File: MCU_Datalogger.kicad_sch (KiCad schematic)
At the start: 0 parts

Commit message: third
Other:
- title: (none) -> ${project_name}
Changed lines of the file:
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@@
 	(generator_version "10.0")
 	(paper "A4")
+	(title_block
+		(title "${project_name}")
+		(date "2026-07-26")
+		(rev "1")
+	)
 	(sheet_instances
 		(path "/"

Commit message: schematic 1
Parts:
- added BT1: Battery, symbol Device:Battery
- added C1, C2, C3, C4: C, symbol Device:C
- added C5: C_Polarized, symbol Device:C_Polarized
- added D1, D2: LED, symbol Device:LED
- added H1, H2, H3, H4: MountingHole, symbol Mechanical:MountingHole
- added R1, R2, R3, R4, R5, R6, R7: R, symbol Device:R
- added U1, U2: 24LC1025, symbol Memory_EEPROM:24LC1025
- added U3: DS1337S_, DS1337S_:SOIC127P600X175-8N, symbol DS1337S_:DS1337S_
- added U4: ATMEGA328P-AU, ATMEGA328P-AU:QFP80P900X900X120-32N, symbol ATMEGA328P-AU:ATMEGA328P-AU
- added Y1, Y2: Crystal, symbol Device:Crystal
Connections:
- new net GND: U4.21 (GND), U4.3 (GND), U4.5 (GND)
- new net VCC: U4.4 (VCC), U4.6 (VCC)

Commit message: aa
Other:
- added sheet Connectors (Connectors.kicad_sch)
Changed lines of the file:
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@@
+		)
+	)
+	(sheet
+		(at 110.744 142.24)
+		(size 39.624 37.084)
+		(exclude_from_sim no)
+		(in_bom yes)
+		(on_board yes)
+		(dnp no)
+		(fields_autoplaced yes)
+		(stroke
+			(width 0.1524)
+			(type solid)
+		)
+		(fill
+			(color 0 0 0 0)
+		)
+		(property "Sheetname" "Connectors"
+			(at 110.744 141.5284 0)
+			(show_name no)
+			(do_not_autoplace no)
+			(effects
+				(font
+					(size 1.27 1.27)
+				)
+				(justify left bottom)
+			)
+		)
+		(property "Sheetfile" "Connectors.kicad_sch"
+			(at 110.744 179.9086 0)
+			(show_name no)
+			(do_not_autoplace no)
+			(effects
+				(font
+					(size 1.27 1.27)
+				)
+				(justify left top)
+			)
+		)
+		(instances
+			(project "MCU_Datalogger"
+				(path "/14fc4073-58ef-4a71-a843-5cc47094620d"
+					(page "2")
+				)
+			)
 		)
 	)

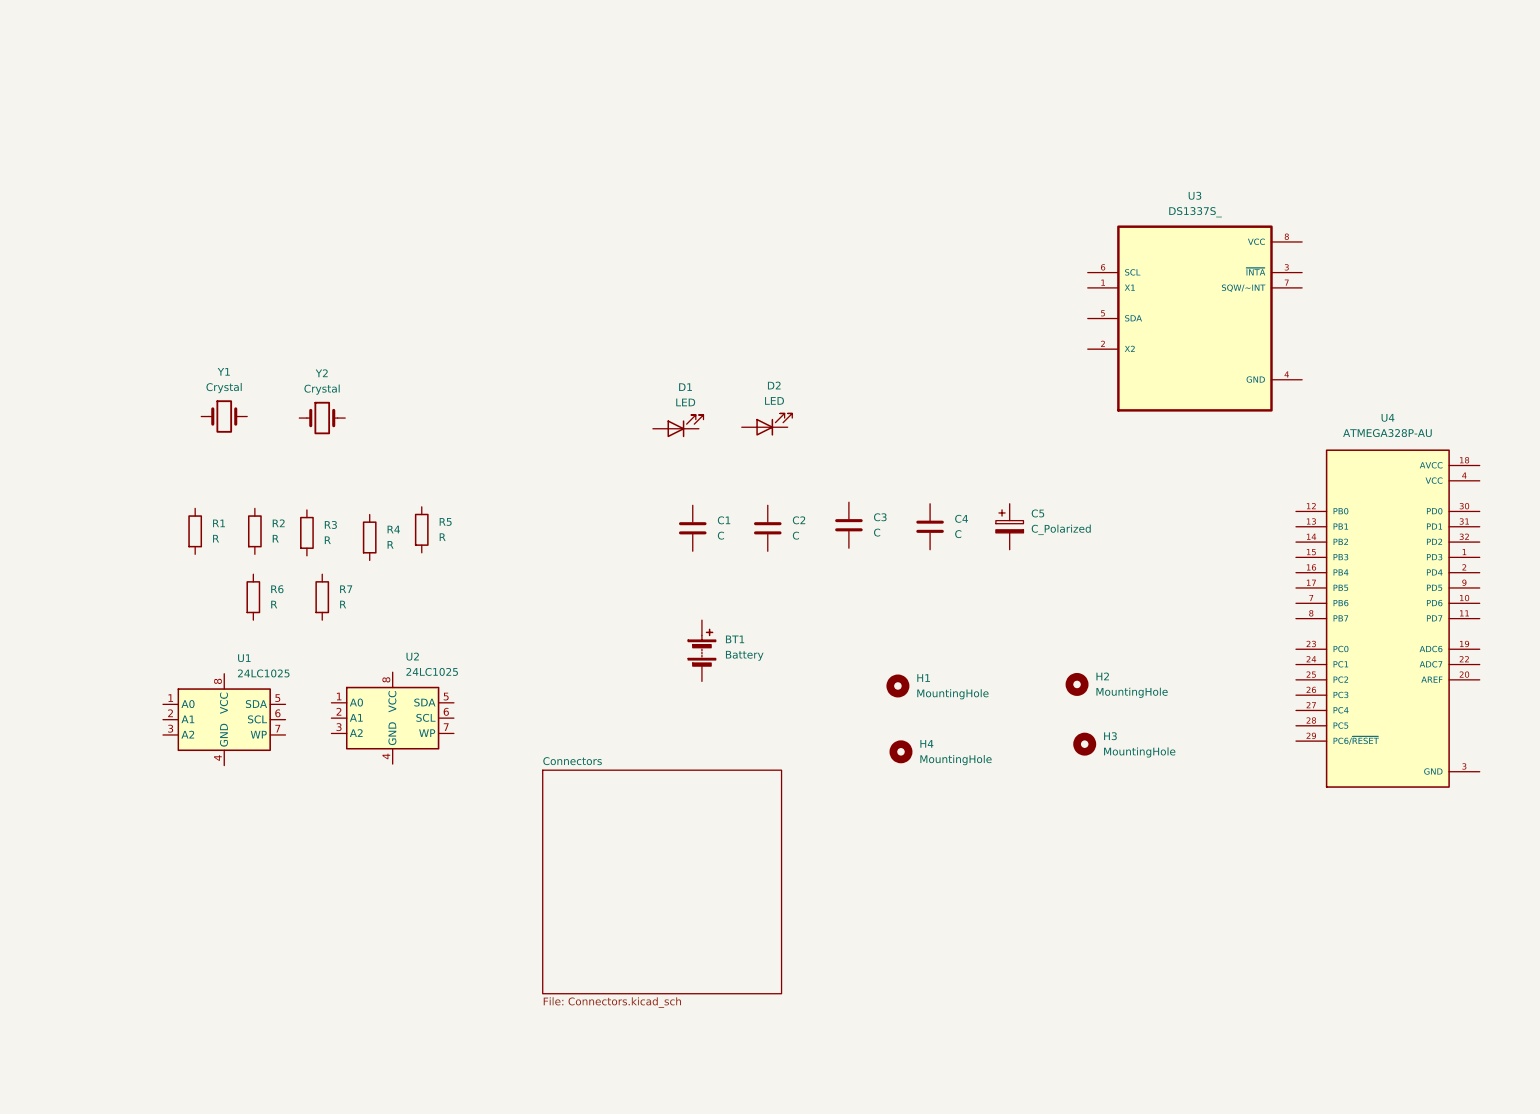
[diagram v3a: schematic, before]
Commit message: main schematic is wired
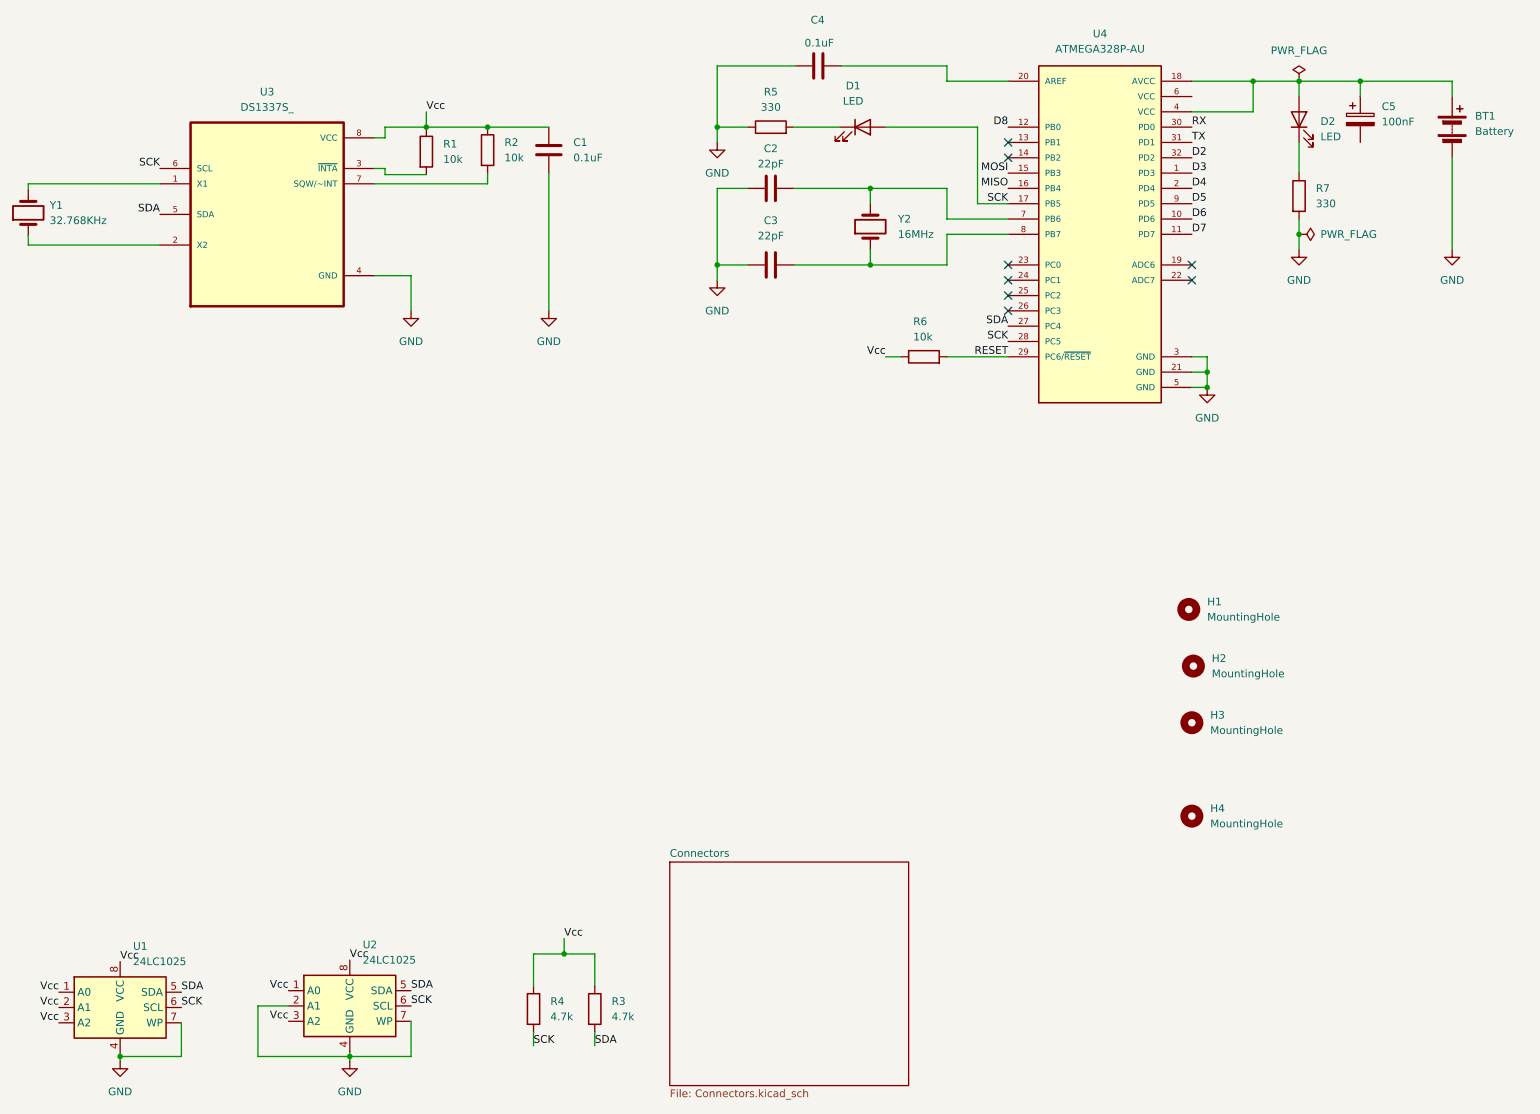
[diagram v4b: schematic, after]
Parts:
- BT1: footprint (none) -> Connector_PinHeader_2.54mm:PinHeader_1x02_P2.54mm_Vertical
- C1, C4: value C -> 0.1uF; footprint (none) -> Capacitor_SMD:C_0805_2012Metric
- C2, C3: value C -> 22pF; footprint (none) -> Capacitor_SMD:C_0805_2012Metric
- C5: value C_Polarized -> 100nF; footprint (none) -> Capacitor_SMD:C_0805_2012Metric
- D1, D2: footprint (none) -> Diode_SMD:D_0805_2012Metric
- H1, H2, H3, H4: footprint (none) -> MountingHole:MountingHole_2.1mm
- R1, R2, R6: value R -> 10k; footprint (none) -> Fuse:Fuse_0805_2012Metric
- R3, R4: value R -> 4.7k; footprint (none) -> Fuse:Fuse_0805_2012Metric
- R5, R7: value R -> 330; footprint (none) -> Fuse:Fuse_0805_2012Metric
- U1, U2: footprint (none) -> Package_SO:SOIC-8_5.3x5.3mm_P1.27mm
- U3: footprint DS1337S_:SOIC127P600X175-8N -> d1337s:SOIC127P600X175-8N
- U4: footprint ATMEGA328P-AU:QFP80P900X900X120-32N -> atmega3288p-au:QFP80P900X900X120-32N
- Y1: value Crystal -> 32.768KHz; footprint (none) -> Crystal:Crystal_SMD_5032-2Pin_5.0x3.2mm_HandSoldering
- Y2: value Crystal -> 16MHz; footprint (none) -> Crystal:Crystal_SMD_5032-2Pin_5.0x3.2mm_HandSoldering
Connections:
- net GND: now also BT1.2 (-), C1.2, C2.1, C3.2, C4.1, R5.1, R7.2, U1.4 (GND), U1.7 (WP), U2.2 (A1), U2.4 (GND), U2.7 (WP), U3.4 (GND)
- net at C3.1: now also U4.8 (PB7), Y2.1
- net Vcc: now reaches U1.1 (A0)
- net Vcc: now also C1.1, R1.1, R2.1, R3.1, R4.1, R6.1, U1.2 (A1), U1.3 (A2), U1.8 (VCC), U2.1 (A0), U2.3 (A2), U2.8 (VCC), U3.8 (VCC)
- net SDA: now reaches U1.5 (SDA)
- net SDA: now also R3.2, U2.5 (SDA), U3.5 (SDA), U4.27 (PC4)
- net SCK: now reaches U1.6 (SCL)
- net SCK: now also D1.2 (A), R4.2, U2.6 (SCL), U3.6 (SCL), U4.17 (PB5), U4.28 (PC5)
- net RESET: now reaches R6.2
- net RESET: now also U4.29 (PC6/~{RESET})
- net at Y1.1: now also U3.2 (X2)
- net at Y1.2: now also U3.1 (X1)
- net at C5.1: now also BT1.1 (+), D2.2 (A), U4.18 (AVCC), U4.4 (VCC)
- net at D1.1 (K): now also R5.2
- net at U3.3 (~{INTA}): now also R1.2
- net at U3.7 (SQW/~INT): now also R2.2
- net D3: now reaches U4.1 (PD3)
- net D6: now reaches U4.10 (PD6)
- net D7: now reaches U4.11 (PD7)
- net D8: now reaches U4.12 (PB0)
- net MOSI: now reaches U4.15 (PB3)
- net MISO: now reaches U4.16 (PB4)
- net D4: now reaches U4.2 (PD4)
- net at U4.20 (AREF): now also C4.2
- net RX: now reaches U4.30 (PD0)
- net TX: now reaches U4.31 (PD1)
- net D2: now reaches U4.32 (PD2)
- net at U4.7 (PB6): now also C2.2, Y2.2
- net D5: now reaches U4.9 (PD5)
- net at D2.1 (K): now also R7.1
- net VCC: no longer names the net of U4.6 (VCC)
- net VCC: no longer U4.4 (VCC)
- no-connect marks 0 -> 8
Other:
- moved on the sheet: BT1, C1, C2, C3, C4, C5, D1, D2, H1, H2, H3, H4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

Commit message: schematic done
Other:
- sheet Connectors ports: added D2, D3, D4, D5, D6, D7, D8, GND, MISO, MOSI, RESET, RX, SCK, SDA, TX, VCC; removed none
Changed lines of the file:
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@@
 	)
 	(sheet
-		(at 131.826 157.48)
-		(size 39.624 37.084)
+		(at 57.912 97.028)
+		(size 59.69 58.674)
 		(exclude_from_sim no)
 		(in_bom yes)
@@
 		)
 		(property "Sheetname" "Connectors"
-			(at 131.826 156.7684 0)
+			(at 57.912 96.3164 0)
 			(show_name no)
 			(do_not_autoplace no)
@@
 		)
 		(property "Sheetfile" "Connectors.kicad_sch"
-			(at 131.826 195.1486 0)
+			(at 57.912 156.2866 0)
 			(show_name no)
 			(do_not_autoplace no)
@@
 			)
 		)
+		(pin "D2" bidirectional
+			(at 117.602 100.33 0)
+			(effects
+				(font
+					(size 1.27 1.27)
+				)
+				(justify right)
+			)
+		)
+		(pin "D3" bidirectional
+			(at 117.602 103.886 0)
+			(effects
+				(font
+					(size 1.27 1.27)
+				)
+				(justify right)
+			)
+		)
+		(pin "D4" bidirectional
+			(at 117.602 106.68 0)
+			(effects
+				(font
+					(size 1.27 1.27)
+				)
+				(justify right)
+			)
+		)
+		(pin "D5" bidirectional
+			(at 117.602 109.22 0)
+			(effects
+				(font
+					(size 1.27 1.27)
+				)
+				(justify right)
+			)
+		)
+		(pin "D6" bidirectional
+			(at 117.602 112.522 0)
+			(effects
+				(font
+					(size 1.27 1.27)
+				)
+				(justify right)
+			)
+		)
+		(pin "D7" bidirectional
+			(at 117.602 115.316 0)
+			(effects
+				(font
+					(size 1.27 1.27)
+				)
+				(justify right)
+			)
+		)
+		(pin "D8" bidirectional
+			(at 117.602 118.364 0)
+			(effects
+				(font
+					(size 1.27 1.27)
+				)
+				(justify right)
+			)
+		)
+		(pin "GND" passive
+			(at 57.912 102.87 180)
+			(effects
+				(font
+					(size 1.27 1.27)
+				)
+				(justify left)
+			)
+		)
+		(pin "MISO" output
+			(at 117.602 147.066 0)
+			(effects
+				(font
+					(size 1.27 1.27)
+				)
+				(justify right)
+			)
+		)
+		(pin "MOSI" input
+			(at 117.602 142.494 0)
+			(effects
+				(font
+					(size 1.27 1.27)
+				)
+				(justify right)
+			)
+		)
+		(pin "RESET" passive
+			(at 117.602 151.892 0)
+			(effects
+				(font
+					(size 1.27 1.27)
+				)
+				(justify right)
+			)
+		)
+		(pin "RX" input
+			(at 57.912 138.938 180)
+			(effects
+				(font
+					(size 1.27 1.27)
+				)
+				(justify left)
+			)
+		)
+		(pin "SCK" passive
+			(at 57.912 129.794 180)
+			(effects
+				(font
+					(size 1.27 1.27)
+				)
+				(justify left)
+			)
+		)
+		(pin "SDA" bidirectional
+			(at 57.912 133.858 180)
+			(effects
+				(font
+					(size 1.27 1.27)
+				)
+				(justify left)
+			)
+		)
+		(pin "TX" output
+			(at 57.912 142.494 180)
+			(effects
+				(font
+					(size 1.27 1.27)
+				)
+				(justify left)
+			)
+		)
+		(pin "VCC" passive
+			(at 57.912 107.696 180)
+			(effects
+				(font
+					(size 1.27 1.27)
+				)
+				(justify left)
+			)
+		)
